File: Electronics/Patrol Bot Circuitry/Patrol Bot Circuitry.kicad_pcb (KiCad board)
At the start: 2 copper layers, 101 x 89.5 mm, 40 parts, among them J1 Left_Motor, J2 Right_Motor, J3 Battery, J4 AC_DC_10V, J5 Servo Motor, Q1 IRF4905, Q2 IRF4905, Q3 IRF4905, Q4 IRLZ44N, U1 ROB-14450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

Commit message: Software Upload 1
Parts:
- removed C1: 0.1u, Capacitor_THT:CP_Axial_L10.0mm_D4.5mm_P15.00mm_Horizontal
- moved R1 3.91 mm to (151.5, 121.0)
- moved D1 3.20 mm to (151.0, 117.5)
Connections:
- U1 pad 13: Net-(U1-Pad13) -> /IO1
- U1 pad 2: /5V -> /3.3V
- U11 pad 12: /IO1 -> Net-(U11-Pad12)
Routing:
- net /IO1: track 12.8 -> 86.3 mm, vias 0 -> 2
- net /3.3V: track 115.4 -> 159.4 mm, vias 2 -> 6
- net /5V: track 233.6 -> 222.1 mm
- net Net-(D1-Pad1): track 38.4 -> 34.4 mm
- net GND: track 59.3 -> 63.1 mm, vias 4 -> 5

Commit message: Validation 1
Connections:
- U11 pad 9: Net-(U11-Pad9) -> GND
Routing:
- net GND: track 63.1 -> 72.5 mm, vias 5 -> 6

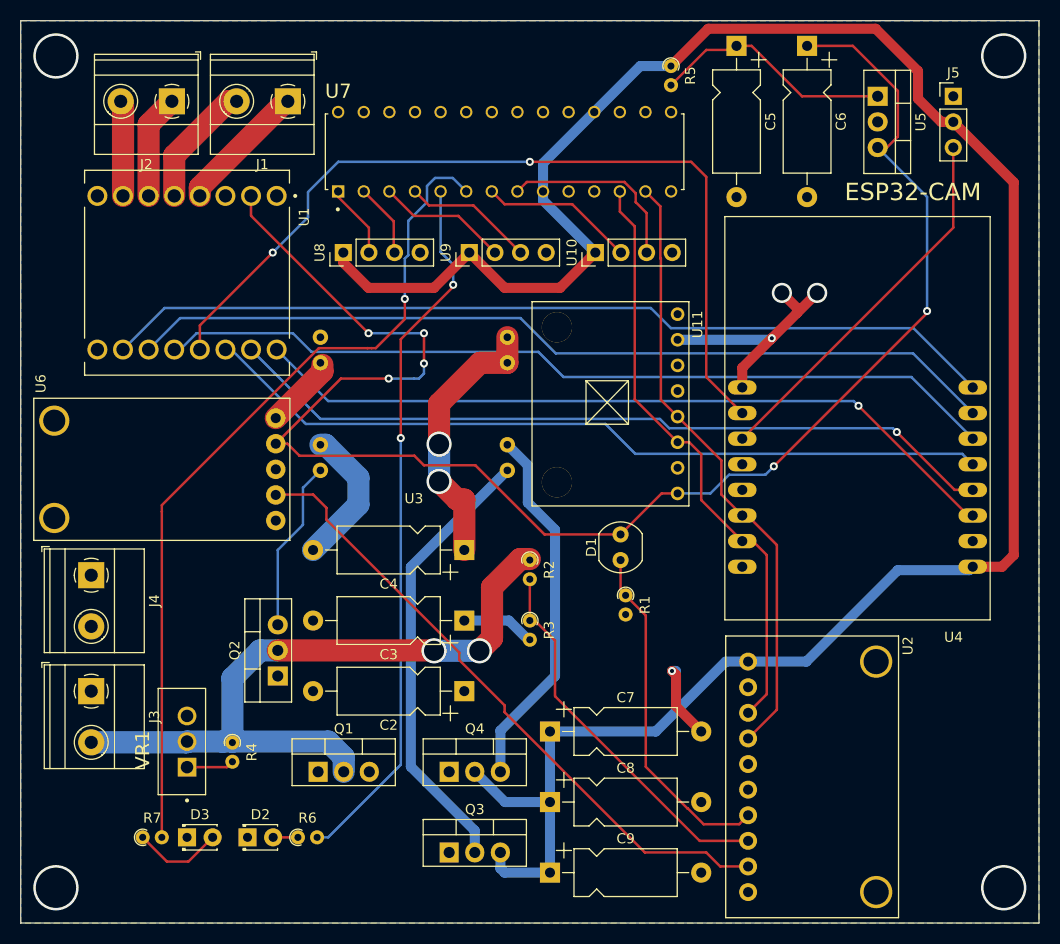
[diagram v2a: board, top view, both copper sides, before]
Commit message: Fixed Power Management Switches
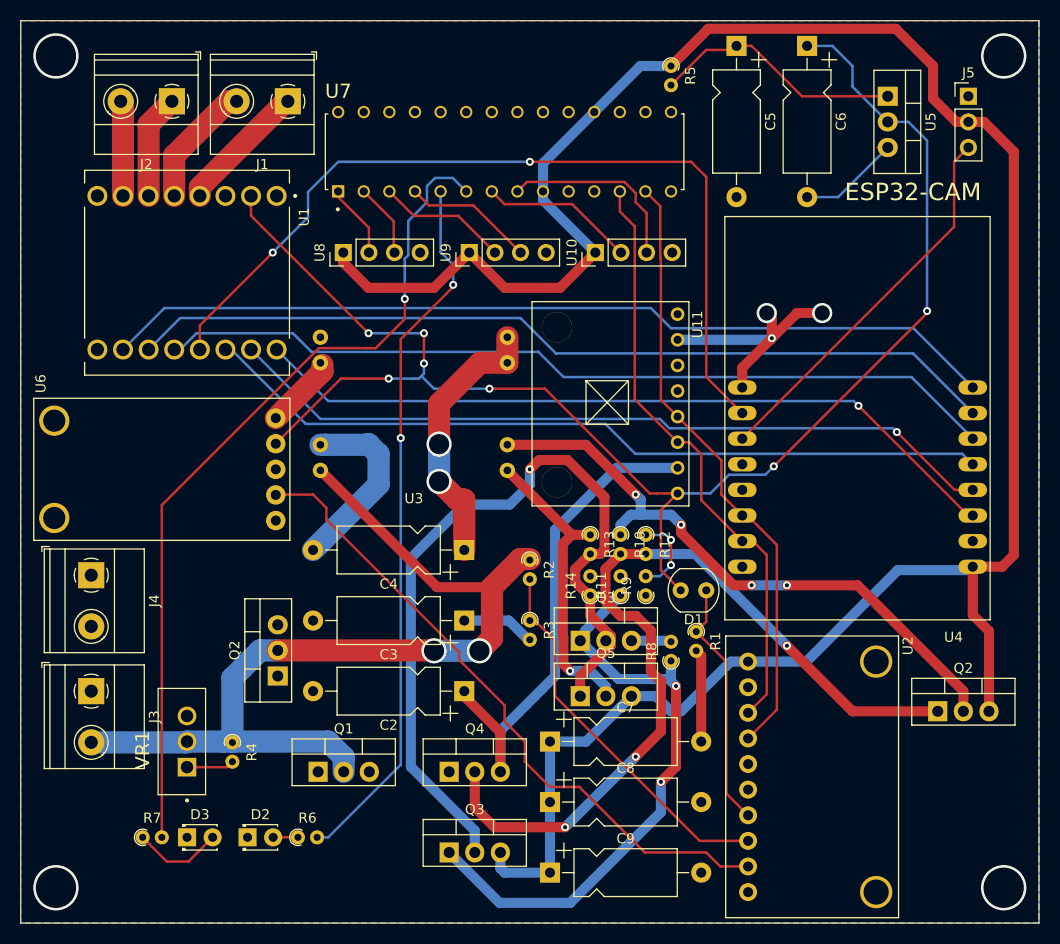
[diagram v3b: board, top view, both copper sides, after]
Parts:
- added Q2: IRF4905, Package_TO_SOT_THT:TO-220-3_Vertical, F.Cu at (182.5, 132.5)
- added Q3: IRF4905, Package_TO_SOT_THT:TO-220-3_Vertical, F.Cu at (147.0, 125.5)
- added Q5: IRF4905, Package_TO_SOT_THT:TO-220-3_Vertical, F.Cu at (147.0, 131.0)
- added R10: 100k, Resistor_THT:R_Axial_DIN0204_L3.6mm_D1.6mm_P1.90mm_Vertical, F.Cu at (151.0, 115.0)
- added R11: 100k, Resistor_THT:R_Axial_DIN0204_L3.6mm_D1.6mm_P1.90mm_Vertical, F.Cu at (151.0, 121.0)
- added R12: 100k, Resistor_THT:R_Axial_DIN0204_L3.6mm_D1.6mm_P1.90mm_Vertical, F.Cu at (153.5, 115.0)
- added R13: 100k, Resistor_THT:R_Axial_DIN0204_L3.6mm_D1.6mm_P1.90mm_Vertical, F.Cu at (148.0, 115.0)
- added R14: 100k, Resistor_THT:R_Axial_DIN0204_L3.6mm_D1.6mm_P1.90mm_Vertical, F.Cu at (148.0, 121.0)
- added R8: 100k, Resistor_THT:R_Axial_DIN0204_L3.6mm_D1.6mm_P1.90mm_Vertical, F.Cu at (156.0, 127.5)
- added R9: 100k, Resistor_THT:R_Axial_DIN0204_L3.6mm_D1.6mm_P1.90mm_Vertical, F.Cu at (153.5, 121.0)
- moved D1 9.01 mm to (159.5, 120.5), turned to 180 degrees
- moved R1 7.87 mm to (158.5, 124.6)
- moved J5 1.50 mm to (185.5, 71.5)
- moved C7 1.00 mm to (144.0, 135.5)
- moved U5 1.00 mm to (177.5, 71.5)
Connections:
- Q4 pad 2: /5V -> Net-(Q2-Pad1)
- Q4 pad 3: Net-(Q4-Pad3) -> GND
- U3 pad 1: Net-(Q3-Pad2) -> Net-(Q5-Pad2)
- U3 pad 2: Net-(Q4-Pad3) -> Net-(Q2-Pad2)
- U3 pad 8: Net-(Q2-Pad3) -> /Battery
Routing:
- net Net-(Q2-Pad1): track 0.00 -> 86.1 mm, vias 0 -> 3
- net GND: track 72.5 -> 145.9 mm, vias 6 -> 7
- net +10V: track 14.2 -> 77.3 mm, vias 0 -> 2
- net Net-(Q2-Pad2): track 0.00 -> 62.1 mm, vias 0 -> 4
- net Net-(Q3-Pad2): track 44.5 -> 81.8 mm, vias 0 -> 1
- net Net-(Q4-Pad3): track 36.6 -> 0.00 mm
- net Net-(Q5-Pad2): track 0.00 -> 30.5 mm, vias 0 -> 1
- net /Battery: track 70.9 -> 92.7 mm
- net Net-(Q2-Pad3): track 17.1 -> 0.00 mm
- net Net-(D1-Pad1): track 34.4 -> 24.9 mm
- net /5V: track 222.1 -> 231.1 mm
- net /3.3V: track 159.4 -> 153.3 mm, vias 6 -> 7
- net /A2: track 63.7 -> 65.4 mm
- net Net-(C5-Pad1): track 24.2 -> 25.2 mm
- net /IO3: track 37.5 -> 38.2 mm

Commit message: Redesigned PCB / Mechanical Drawing
ESP32-cam not connecting to Wifi -> must DEBUG
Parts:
- removed the Q2 at (182.5, 132.5)
- removed the Q2 at (117.0, 129.0)
- removed the Q3 at (147.0, 125.5)
- removed the Q3 at (134.0, 146.5)
- removed R14: 100k, Resistor_THT:R_Axial_DIN0204_L3.6mm_D1.6mm_P1.90mm_Vertical
- removed R5: 30, Resistor_THT:R_Axial_DIN0204_L3.6mm_D1.6mm_P1.90mm_Vertical
- added C1: 0.47u, Capacitor_SMD:C_0603_1608Metric, F.Cu at (133.2, 80.8)
- added Q2: Q_PMOS_GSD, Package_TO_SOT_SMD:SOT-23, F.Cu at (145.3, 94.6)
- added Q3: Q_NMOS_GSD, Package_TO_SOT_SMD:SOT-23, F.Cu at (130.6, 94.5)
- C2: value 20n -> 0.01n; footprint Capacitor_THT:CP_Axial_L10.0mm_D4.5mm_P15.00mm_Horizontal -> Capacitor_SMD:C_0603_1608Metric
- C3, C8: value 20n -> 0.1u; footprint Capacitor_THT:CP_Axial_L10.0mm_D4.5mm_P15.00mm_Horizontal -> Capacitor_SMD:C_0603_1608Metric
- C4, C7: value 20n -> 0.47u; footprint Capacitor_THT:CP_Axial_L10.0mm_D4.5mm_P15.00mm_Horizontal -> Capacitor_SMD:C_0603_1608Metric
- C5, C6: footprint Capacitor_THT:CP_Axial_L10.0mm_D4.5mm_P15.00mm_Horizontal -> Capacitor_THT:CP_Radial_D7.5mm_P2.50mm
- C9: value 20n -> 0.01u; footprint Capacitor_THT:CP_Axial_L10.0mm_D4.5mm_P15.00mm_Horizontal -> Capacitor_SMD:C_0603_1608Metric
- D2, D3: footprint LED_THT:LED_D1.8mm_W3.3mm_H2.4mm -> LED_THT:LED_D3.0mm
- Q1: value IRF4905 -> Q_NMOS_GSD; footprint Package_TO_SOT_THT:TO-220-3_Vertical -> Package_TO_SOT_SMD:SOT-23
- Q4: value IRLZ44N -> Q_PMOS_GSD; footprint Package_TO_SOT_THT:TO-220-3_Vertical -> Package_TO_SOT_SMD:SOT-23
- Q5: value IRF4905 -> Q_PMOS_GSD; footprint Package_TO_SOT_THT:TO-220-3_Vertical -> Package_TO_SOT_SMD:SOT-23
- R1: value 100K -> 200K; footprint Resistor_THT:R_Axial_DIN0204_L3.6mm_D1.6mm_P1.90mm_Vertical -> Resistor_SMD:R_0603_1608Metric
- R10, R11, R12, R13, R8, R9: value 100k -> 200k; footprint Resistor_THT:R_Axial_DIN0204_L3.6mm_D1.6mm_P1.90mm_Vertical -> Resistor_SMD:R_0603_1608Metric
- R2: value 600K -> 620K; footprint Resistor_THT:R_Axial_DIN0204_L3.6mm_D1.6mm_P1.90mm_Vertical -> Resistor_SMD:R_0603_1608Metric
- R3, R4, R6, R7: footprint Resistor_THT:R_Axial_DIN0204_L3.6mm_D1.6mm_P1.90mm_Vertical -> Resistor_SMD:R_0603_1608Metric
- U11: footprint MPU-6050:QFN50P400X400X95-24N -> Connector_PinSocket_2.54mm:PinSocket_1x08_P2.54mm_Vertical
- U2: footprint ADS1115:ADS1115 -> Connector_PinSocket_2.54mm:PinSocket_1x10_P2.54mm_Vertical
- U3: moved to B.Cu
- U6: footprint MAX9814:MAX9814 -> Connector_PinSocket_2.54mm:PinSocket_1x05_P2.54mm_Vertical
- U7: value MCP23017-E_SP -> PCF8574; footprint MCP23017:DIP787W45P254L3556H508Q28 -> PCF8574N:DIP794W45P254L1969H508Q16
- moved D3 96.5 mm to (183.1, 84.3), turned to 90 degrees
- moved R7 89.8 mm to (167.3, 81.7), turned to 180 degrees
- moved D2 87.1 mm to (182.9, 91.7), turned to 90 degrees
- moved R6 81.6 mm to (170.4, 81.7), turned to 180 degrees
- moved C5 77.4 mm to (117.5, 129.6), turned to 0 degrees
- moved C6 75.5 mm to (125.7, 128.0), turned to 0 degrees
- moved U2 71.8 mm to (124.6, 83.4), turned to 90 degrees
- moved J5 69.5 mm to (142.1, 125.8), turned to 90 degrees
- moved VR1 69.1 mm to (176.2, 124.3), turned to 0 degrees
- moved U5 63.7 mm to (125.1, 107.8), turned to 90 degrees
- moved R4 62.6 mm to (142.9, 80.8), turned to 0 degrees
- moved U8 55.0 mm to (178.4, 83.6), turned to 0 degrees
- moved Q1 48.6 mm to (141.8, 94.6)
- moved C9 47.3 mm to (140.2, 101.4)
- moved J1 45.1 mm to (115.7, 117.0), turned to 270 degrees
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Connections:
- C2 pad 2: +10V -> /Battery
- C3 pad 2: +10V -> /Battery
- C4 pad 2: +10V -> /Battery
- C5 pad 1: Net-(C5-Pad1) -> +5V
- C7 pad 1: /5V -> +5V
- C8 pad 1: /5V -> +5V
- C9 pad 1: /5V -> +5V
- J5 pad 2: /5V -> +5V
- Q1 pad 2: /Battery -> GND
- Q1 pad 3: +10V -> Net-(Q1-Pad3)
- Q4 pad 1: +10V -> Net-(Q3-Pad3)
- Q4 pad 2: Net-(Q2-Pad1) -> Net-(Q4-Pad2)
- Q4 pad 3: GND -> Net-(Q4-Pad3)
- Q5 pad 1: Net-(Q3-Pad2) -> Net-(Q4-Pad3)
- Q5 pad 2: Net-(Q5-Pad2) -> Net-(Q4-Pad2)
- Q5 pad 3: /5V -> +5V
- R10 pad 2: Net-(Q2-Pad1) -> Net-(Q1-Pad3)
- R12 pad 1: GND -> Net-(Q4-Pad3)
- R12 pad 2: Net-(Q2-Pad1) -> GND
- R13 pad 1: Net-(Q5-Pad2) -> Net-(Q4-Pad2)
- R13 pad 2: Net-(Q3-Pad2) -> Net-(Q3-Pad3)
- U1 pad 1: +10V -> /Battery
- U10 pad 1: /5V -> +5V
- U11 pad 7: Net-(U11-Pad7) -> GND
- U2 pad 1: /5V -> +5V
- U3 pad 1: Net-(Q5-Pad2) -> Net-(Q4-Pad2)
- U4 pad P$1: /5V -> +5V
- U5 pad 1: Net-(C5-Pad1) -> +5V
- U7 pad 1: Net-(U7-Pad1) -> GND
- U7 pad 10: GND -> Net-(R7-Pad2)
- U7 pad 11: (no net) -> Net-(U10-Pad2)
- U7 pad 12: /SCL -> Net-(U10-Pad3)
- U7 pad 13: /SDA -> Net-(U7-Pad13)
- U7 pad 14: (no net) -> /SCL
- U7 pad 15: GND -> /SDA
- U7 pad 16: GND -> +5V
- U7 pad 2: Net-(U7-Pad2) -> GND
- U7 pad 3: Net-(U7-Pad3) -> GND
- U7 pad 5: Net-(R6-Pad2) -> Net-(U7-Pad5)
- U7 pad 6: Net-(R7-Pad2) -> Net-(U7-Pad6)
- U7 pad 7: Net-(U10-Pad2) -> Net-(U7-Pad7)
- U7 pad 8: Net-(U10-Pad3) -> GND
- U7 pad 9: /5V -> Net-(R6-Pad2)
- U8 pad 1: /5V -> +5V
- U8 pad 2: Net-(U7-Pad1) -> Net-(U7-Pad4)
- U8 pad 3: Net-(U7-Pad2) -> Net-(U7-Pad5)
- U9 pad 1: /5V -> +5V
- U9 pad 2: Net-(U7-Pad3) -> Net-(U7-Pad6)
- U9 pad 3: Net-(U7-Pad4) -> Net-(U7-Pad7)
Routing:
- net +5V: track 0.00 -> 312.3 mm, vias 0 -> 7
- net /5V: track 231.1 -> 0.00 mm
- net +10V: track 77.3 -> 194.7 mm, vias 2 -> 7
- net Net-(D1-Pad1): track 24.9 -> 125.6 mm, vias 0 -> 2
- net Net-(Q4-Pad2): track 0.00 -> 98.3 mm, vias 0 -> 8
- net Net-(Q2-Pad1): track 86.1 -> 0.00 mm, vias 3 -> 0
- net Net-(Q3-Pad2): track 81.8 -> 0.00 mm, vias 1 -> 0
- net Net-(U1-Pad11): track 86.9 -> 21.5 mm
- net Net-(U1-Pad10): track 89.3 -> 24.6 mm
- net Net-(R4-Pad2): track 4.72 -> 69.0 mm
- net Net-(U1-Pad14): track 78.8 -> 20.7 mm, vias 0 -> 1
- net Net-(U1-Pad12): track 84.2 -> 30.6 mm, vias 0 -> 3
- net Net-(R7-Pad2): track 83.6 -> 30.4 mm, vias 1 -> 0
- net Net-(U1-Pad16): track 75.9 -> 30.8 mm, vias 1 -> 2
- net Net-(U1-Pad15): track 77.3 -> 35.2 mm
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- added copper zone on F.Cu, net /Battery
- removed copper zone on F.Cu, net +10V
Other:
- board size 101 x 89.5 mm -> 78 x 56.6 mm
